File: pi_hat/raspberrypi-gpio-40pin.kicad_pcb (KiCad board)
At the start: 2 copper layers, 86.8 x 70.1 mm, 83 parts, among them J1 MC000052, J2 10pinIDC, J3 MOLEX_2031, P1 Conn_02x20_Odd_Even, Q1 IRLB8721PBF, SW1 SW_Push, U1 iCE40-HX4K-TQ144, U2 MCP1826S-3302E/DB, U3 MCP1826S-1202E/DB, U4 S25FL064LABMFI010, Y1 SIT8008BI-12-XXE-100

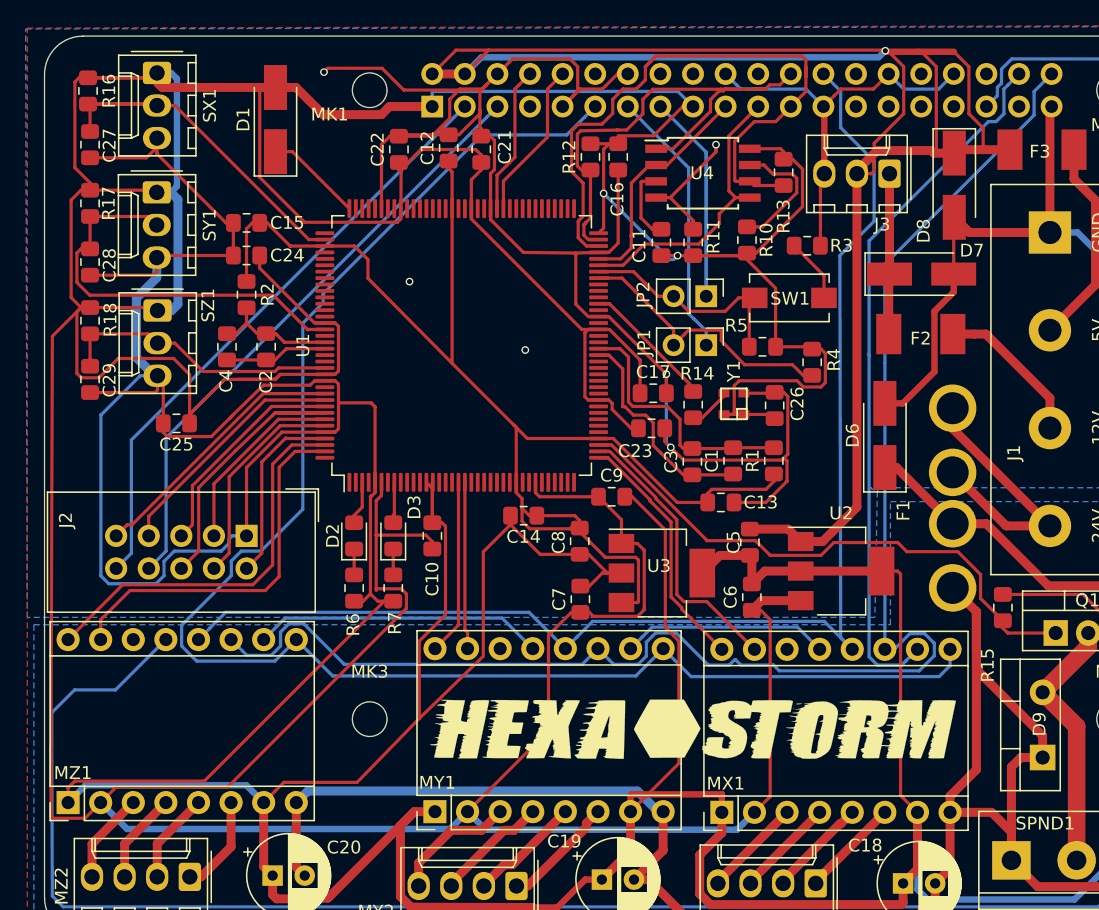
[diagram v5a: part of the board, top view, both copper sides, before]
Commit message: improved pcb
made pincompatible with icezero SPI ports
simplified PCB, reduced capacitors and removed 3V creator
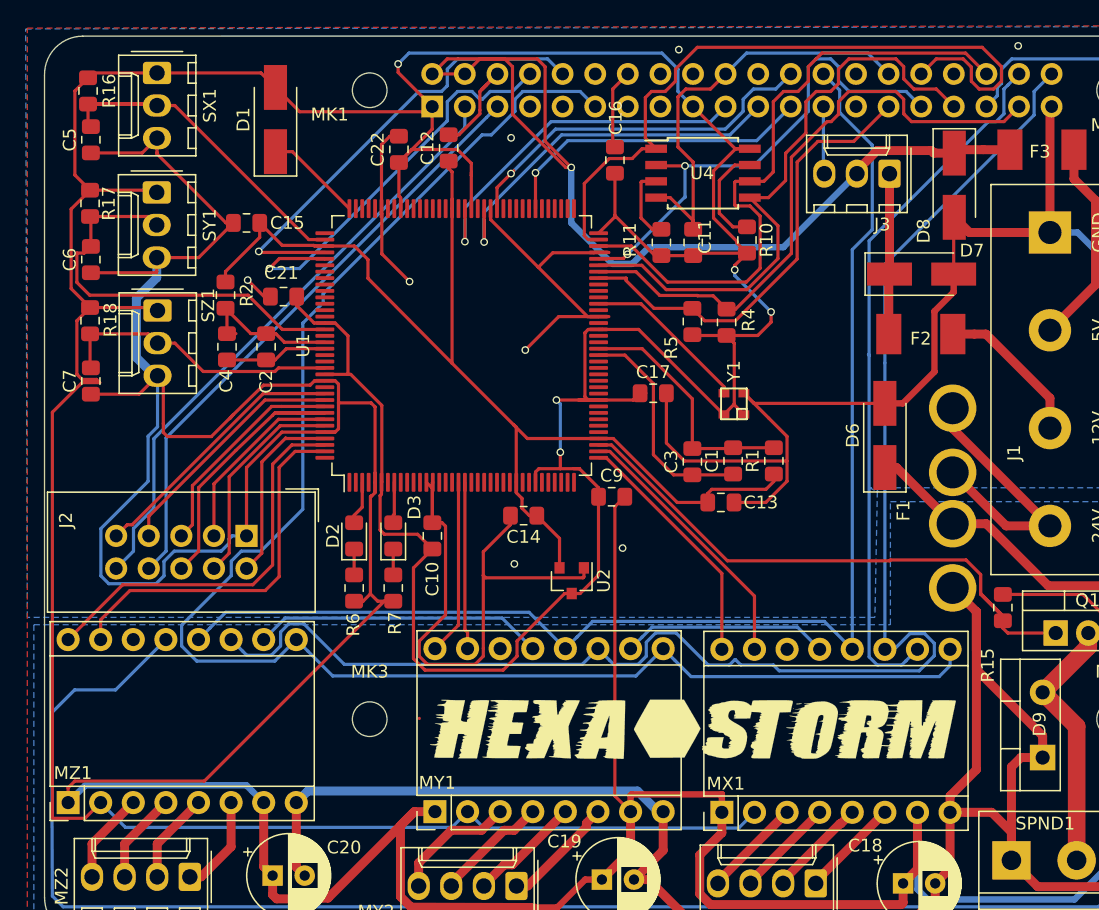
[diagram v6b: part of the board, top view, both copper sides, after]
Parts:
- removed C23, C24, C25, C26, C27, C28, C29: 0.1uF, Capacitor_SMD:C_0805_2012Metric_Pad1.15x1.40mm_HandSolder
- removed C8: 4.7uF, Capacitor_SMD:C_0805_2012Metric_Pad1.15x1.40mm_HandSolder
- removed JP1, JP2: Jumper, Connector_PinHeader_2.54mm:PinHeader_1x02_P2.54mm_Vertical
- removed R12, R13: 4.7K, Resistor_SMD:R_0805_2012Metric_Pad1.15x1.40mm_HandSolder
- removed R14: 220, Resistor_SMD:R_0805_2012Metric_Pad1.15x1.40mm_HandSolder
- removed R3: 100, Resistor_SMD:R_0805_2012Metric_Pad1.15x1.40mm_HandSolder
- removed SW1: SW_Push, Button_Switch_SMD:SW_SPST_EVQPE1
- removed U3: MCP1826S-1202E/DB, Package_TO_SOT_SMD:SOT-223
- C5, C6, C7: value 4.7uF -> 0.1uF
- R10, R11, R4, R5: value 4.7K -> 10K
- U2: value MCP1826S-3302E/DB -> MCP1700-1202E_SOT23; footprint Package_TO_SOT_SMD:SOT-223 -> Package_TO_SOT_SMD:SOT-23
- moved C5 60.2 mm to (181.8, 101.4), turned to 90 degrees
- moved C6 57.8 mm to (181.8, 110.7)
- moved C7 41.8 mm to (181.8, 120.2)
- moved U2 21.0 mm to (219.2, 135.7), turned to 270 degrees
- moved C21 19.2 mm to (196.8, 113.6), turned to 180 degrees
- moved R4 7.36 mm to (231.3, 115.6)
- moved R5 5.80 mm to (228.6, 115.5), turned to 90 degrees
- moved R2 1.64 mm to (192.3, 113.5)
- moved C16 0.36 mm to (222.6, 102.9), turned to 90 degrees
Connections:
- C5 pad 1: +5V -> GND
- C5 pad 2: GND -> X_PO
- C6 pad 1: +3V3 -> GND
- C6 pad 2: GND -> Y_PO
- C7 pad 1: +3V3 -> GND
- C7 pad 2: GND -> Z_PO
- MX1 pad 6: Net-(MX1-Pad6) -> (no net)
- MY1 pad 6: Net-(MY1-Pad6) -> (no net)
- MZ1 pad 6: Net-(MZ1-Pad6) -> (no net)
- P1 pad 10: GPIO15 -> PI_UART_RO
- P1 pad 12: Net-(P1-Pad12) -> (no net)
- P1 pad 13: RP_CDONE -> (no net)
- P1 pad 15: RP_CRESET -> (no net)
- P1 pad 16: Net-(P1-Pad16) -> (no net)
- P1 pad 18: Net-(P1-Pad18) -> (no net)
- P1 pad 19: SPI0_DI -> PI_SPI_MOSI
- P1 pad 21: SPI0_DO -> PI_SPI_MISO
- P1 pad 22: Net-(P1-Pad22) -> (no net)
- P1 pad 23: SPI0_SCL -> PI_SPI_SCK
- P1 pad 24: SPI0_CE -> PI_SPI_CE_0
- P1 pad 27: Net-(P1-Pad27) -> (no net)
- P1 pad 28: Net-(P1-Pad28) -> (no net)
- P1 pad 29: Net-(P1-Pad29) -> CFG_DONE
- P1 pad 31: Net-(P1-Pad31) -> CFG_SI
- P1 pad 32: Net-(P1-Pad32) -> CFG_SS
- P1 pad 33: Net-(P1-Pad33) -> CFG_SO
- P1 pad 36: Net-(P1-Pad36) -> CFG_SCK
- P1 pad 37: Net-(P1-Pad37) -> CFG_RST
- P1 pad 7: Net-(P1-Pad7) -> (no net)
- P1 pad 8: GPIO14 -> PI_UART_WI
- R4 pad 1: ICE40_CDONE -> +3V3
- R4 pad 2: +3V3 -> CFG_RST
- R5 pad 1: ICE40_CRESET -> +3V3
- R5 pad 2: +3V3 -> CFG_DONE
- U1 pad 1: Net-(U1-Pad1) -> (no net)
- U1 pad 10: Net-(U1-Pad10) -> (no net)
- U1 pad 101: Net-(U1-Pad101) -> (no net)
- U1 pad 102: Net-(U1-Pad102) -> (no net)
- U1 pad 104: Net-(U1-Pad104) -> (no net)
- U1 pad 105: Net-(U1-Pad105) -> (no net)
- U1 pad 106: Net-(U1-Pad106) -> (no net)
- U1 pad 107: Net-(U1-Pad107) -> (no net)
- U1 pad 109: Net-(U1-Pad109) -> (no net)
- U1 pad 11: Net-(U1-Pad11) -> (no net)
- U1 pad 112: Net-(U1-Pad112) -> PI_UART_RO
- U1 pad 113: Net-(U1-Pad113) -> PI_UART_WI
- U1 pad 114: Net-(U1-Pad114) -> (no net)
- U1 pad 115: Net-(U1-Pad115) -> (no net)
- U1 pad 116: Net-(U1-Pad116) -> (no net)
- U1 pad 117: Net-(U1-Pad117) -> (no net)
- U1 pad 118: Net-(U1-Pad118) -> (no net)
- U1 pad 119: Net-(U1-Pad119) -> (no net)
- U1 pad 12: Net-(U1-Pad12) -> (no net)
- U1 pad 120: Net-(U1-Pad120) -> (no net)
- U1 pad 121: Net-(U1-Pad121) -> (no net)
- U1 pad 122: Net-(U1-Pad122) -> (no net)
- U1 pad 125: Net-(U1-Pad125) -> (no net)
- U1 pad 128: Net-(U1-Pad128) -> (no net)
- U1 pad 129: Net-(U1-Pad129) -> (no net)
- U1 pad 133: Net-(U1-Pad133) -> (no net)
- U1 pad 144: Net-(U1-Pad144) -> (no net)
- U1 pad 15: Net-(U1-Pad15) -> (no net)
- U1 pad 16: Net-(U1-Pad16) -> (no net)
- U1 pad 17: Net-(U1-Pad17) -> (no net)
- U1 pad 2: Net-(U1-Pad2) -> (no net)
- U1 pad 20: Net-(U1-Pad20) -> (no net)
- U1 pad 21: Net-(U1-Pad21) -> (no net)
- U1 pad 22: Net-(U1-Pad22) -> (no net)
- U1 pad 23: Net-(U1-Pad23) -> (no net)
- U1 pad 24: Net-(U1-Pad24) -> (no net)
- U1 pad 25: Net-(U1-Pad25) -> (no net)
- U1 pad 26: Net-(U1-Pad26) -> (no net)
- U1 pad 28: Net-(U1-Pad28) -> (no net)
- U1 pad 29: Net-(U1-Pad29) -> (no net)
- U1 pad 31: Net-(U1-Pad31) -> (no net)
- U1 pad 32: Net-(U1-Pad32) -> (no net)
- U1 pad 33: Net-(U1-Pad33) -> (no net)
- U1 pad 34: Net-(U1-Pad34) -> (no net)
- U1 pad 35: Net-(U1-Pad35) -> (no net)
- U1 pad 36: Net-(U1-Pad36) -> (no net)
- U1 pad 4: Net-(U1-Pad4) -> (no net)
- U1 pad 41: Net-(U1-Pad41) -> (no net)
- U1 pad 42: Net-(U1-Pad42) -> (no net)
- U1 pad 43: Net-(U1-Pad43) -> (no net)
- U1 pad 44: Net-(U1-Pad44) -> (no net)
- U1 pad 45: Net-(U1-Pad45) -> (no net)
- U1 pad 47: Net-(U1-Pad47) -> (no net)
- U1 pad 48: Net-(U1-Pad48) -> (no net)
- U1 pad 49: Net-(U1-Pad49) -> (no net)
- U1 pad 50: Net-(U1-Pad50) -> (no net)
- U1 pad 51: Net-(U1-Pad51) -> (no net)
- U1 pad 52: Net-(U1-Pad52) -> (no net)
- U1 pad 55: Net-(U1-Pad55) -> (no net)
- U1 pad 56: Net-(U1-Pad56) -> (no net)
- U1 pad 58: Net-(U1-Pad58) -> (no net)
- U1 pad 60: Net-(U1-Pad60) -> (no net)
- U1 pad 62: Net-(U1-Pad62) -> (no net)
- U1 pad 63: Net-(U1-Pad63) -> (no net)
- U1 pad 64: Net-(U1-Pad64) -> (no net)
- U1 pad 65: ICE40_CDONE -> CFG_DONE
- U1 pad 66: ICE40_CRESET -> CFG_RST
- U1 pad 67: SPI0_DO -> CFG_SO
- U1 pad 68: SPI0_DI -> CFG_SI
- U1 pad 7: Net-(U1-Pad7) -> (no net)
- U1 pad 70: SPI0_SCL -> CFG_SCK
- U1 pad 71: SPI0_CE -> CFG_SS
- U1 pad 73: Net-(U1-Pad73) -> (no net)
- U1 pad 74: Net-(U1-Pad74) -> (no net)
- U1 pad 75: Net-(U1-Pad75) -> (no net)
- U1 pad 76: Net-(U1-Pad76) -> (no net)
- U1 pad 77: Net-(U1-Pad77) -> (no net)
- U1 pad 78: Net-(U1-Pad78) -> (no net)
- U1 pad 79: Net-(U1-Pad79) -> PI_SPI_SCK
- U1 pad 80: Net-(U1-Pad80) -> (no net)
- U1 pad 81: Net-(U1-Pad81) -> (no net)
- U1 pad 82: Net-(U1-Pad82) -> (no net)
- U1 pad 83: Net-(U1-Pad83) -> (no net)
- U1 pad 84: GPIO15 -> (no net)
- U1 pad 85: GPIO14 -> PI_SPI_CE_0
- U1 pad 87: Net-(U1-Pad87) -> PI_SPI_MISO
- U1 pad 88: Net-(U1-Pad88) -> (no net)
- U1 pad 9: Net-(U1-Pad9) -> (no net)
- U1 pad 90: Net-(U1-Pad90) -> PI_SPI_MOSI
- U1 pad 91: Net-(U1-Pad91) -> (no net)
- U1 pad 93: Net-(U1-Pad93) -> (no net)
- U1 pad 94: Net-(U1-Pad94) -> (no net)
- U1 pad 95: Net-(U1-Pad95) -> (no net)
- U1 pad 96: Net-(U1-Pad96) -> (no net)
- U1 pad 97: Net-(U1-Pad97) -> (no net)
- U1 pad 98: Net-(U1-Pad98) -> (no net)
- U1 pad 99: Net-(U1-Pad99) -> (no net)
- U2 pad 1: +5V -> GND
- U2 pad 2: GND -> +1V2
- U4 pad 1: SPI0_CE -> CFG_SS
- U4 pad 2: SPI0_DI -> CFG_SI
- U4 pad 5: SPI0_DO -> CFG_SO
- U4 pad 6: SPI0_SCL -> CFG_SCK
- Y1 pad 3: Net-(R14-Pad2) -> OSC_OUT
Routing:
- net +3V3: track 528.0 -> 369.5 mm, vias 2 -> 5
- net GND: track 713.4 -> 604.6 mm, vias 6 -> 8
- net +5V: track 160.0 -> 80.5 mm
- net CFG_SS: track 0.00 -> 56.6 mm
- net SPI0_SCL: track 51.0 -> 0.00 mm
- net CFG_SCK: track 0.00 -> 50.7 mm
- net CFG_RST: track 0.00 -> 48.1 mm
- net CFG_SO: track 0.00 -> 47.2 mm
- net CFG_SI: track 0.00 -> 39.6 mm, vias 0 -> 2
- net SPI0_CE: track 39.1 -> 0.00 mm
- net PI_UART_RO: track 0.00 -> 36.3 mm, vias 0 -> 1
- net CFG_DONE: track 0.00 -> 35.4 mm
- net PI_UART_WI: track 0.00 -> 32.6 mm, vias 0 -> 1
- net PI_SPI_MISO: track 0.00 -> 29.7 mm, vias 0 -> 1
- net PI_SPI_CE_0: track 0.00 -> 29.1 mm, vias 0 -> 1
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
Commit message: new version of board
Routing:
- net GND: vias 8 -> 10
